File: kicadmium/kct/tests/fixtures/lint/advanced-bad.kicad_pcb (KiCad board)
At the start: 2 copper layers, 120 x 120 mm, 13 parts, among them J1 10k, P1 10k, P2 10k, U1 10k, U2 10k

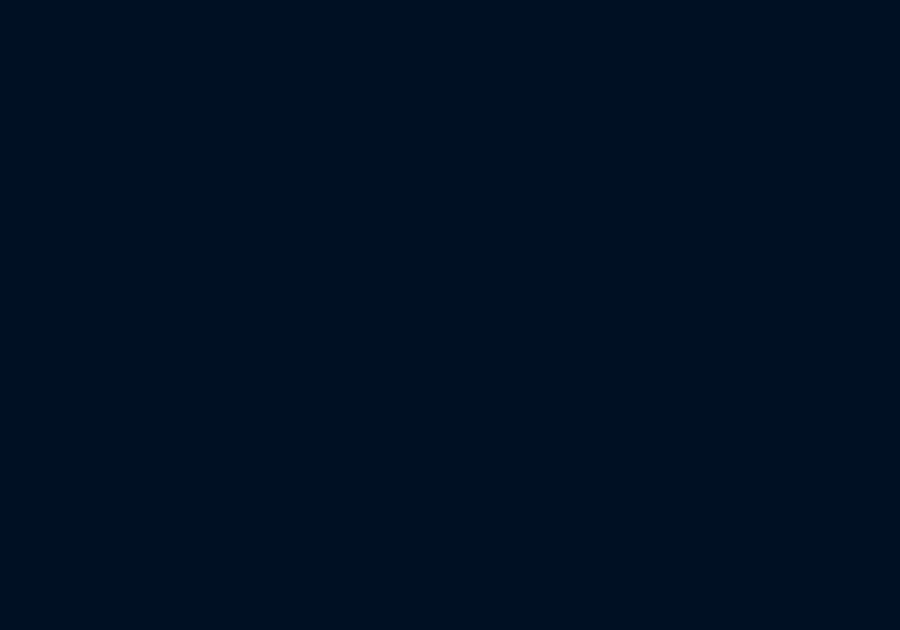
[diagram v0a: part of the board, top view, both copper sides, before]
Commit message: kct lint: route.redundant_bend flags same-length zig-zags
An unbranched chain whose bends can be reduced by moving one leg earlier
or later: the legs in between shift by that leg, taking the other two
sides of the parallelogram they span. Endpoints, leg directions and length
are unchanged; a candidate must remove a bend, create no sharper corner,
keep every via/pad/branch contact, and pass the same clearance, edge and
keepout screen as route.legal_shortcut. Changing a chain end's direction
(a diagonal pad exit) is only offered when the chain backtracks along an
axis, so monotone doglegs are never flagged; legs or runs shorter than
short_segment_mm are left to trace.short_segment.

Co-Authored-By: Claude Opus 5.5 <noreply@anthropic.com>
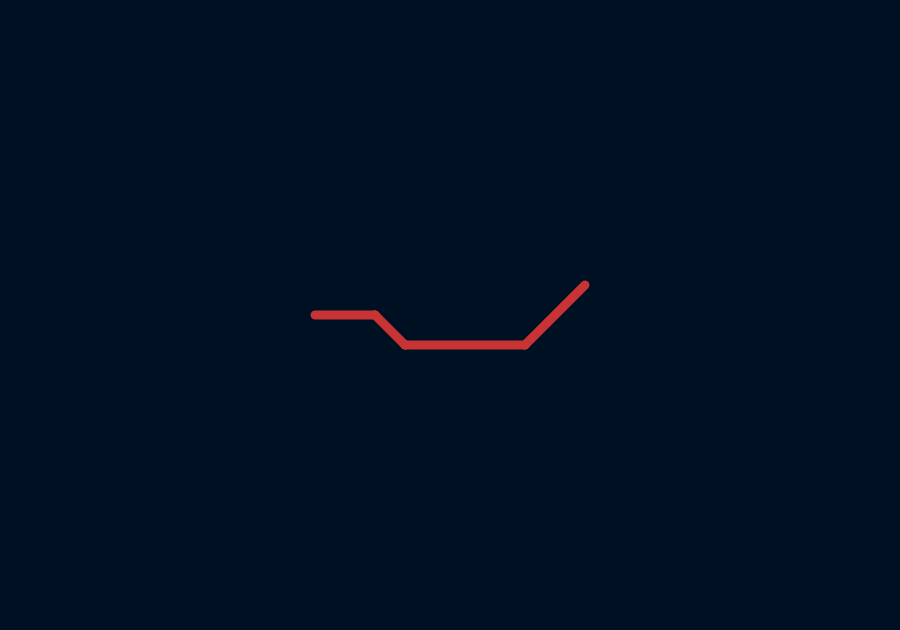
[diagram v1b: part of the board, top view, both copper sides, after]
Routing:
- net ZAG: track 0.00 -> 10.2 mm
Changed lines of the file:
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@@
 (segment (start 75 15) (end 72 15) (width 0.3) (layer "F.Cu") (net "REV") (uuid "rev3"))
 (segment (start 72 15) (end 72 12) (width 0.3) (layer "F.Cu") (net "REV") (uuid "rev4"))
+(segment (start 80 70) (end 82 70) (width 0.3) (layer "F.Cu") (net "ZAG") (uuid "zag0"))
+(segment (start 82 70) (end 83 71) (width 0.3) (layer "F.Cu") (net "ZAG") (uuid "zag1"))
+(segment (start 83 71) (end 87 71) (width 0.3) (layer "F.Cu") (net "ZAG") (uuid "zag2"))
+(segment (start 87 71) (end 89 69) (width 0.3) (layer "F.Cu") (net "ZAG") (uuid "zag3"))
 (segment (start 99 0) (end 102 0) (width 0.3) (layer "F.Cu") (net "E") (uuid "edgefail"))
 (gr_text "U1" (at 0 30) (layer "F.SilkS") (uuid "txt") (effects (font (size 1 1))))
